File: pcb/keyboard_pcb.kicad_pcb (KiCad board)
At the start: 2 copper layers, 144.8 x 98.6 mm, 23 parts, among them J1 TRRS, K00 KEYSW, K01 KEYSW, K02 KEYSW, K03 KEYSW, K04 KEYSW, K05 KEYSW, K10 KEYSW, K11 KEYSW, K12 KEYSW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

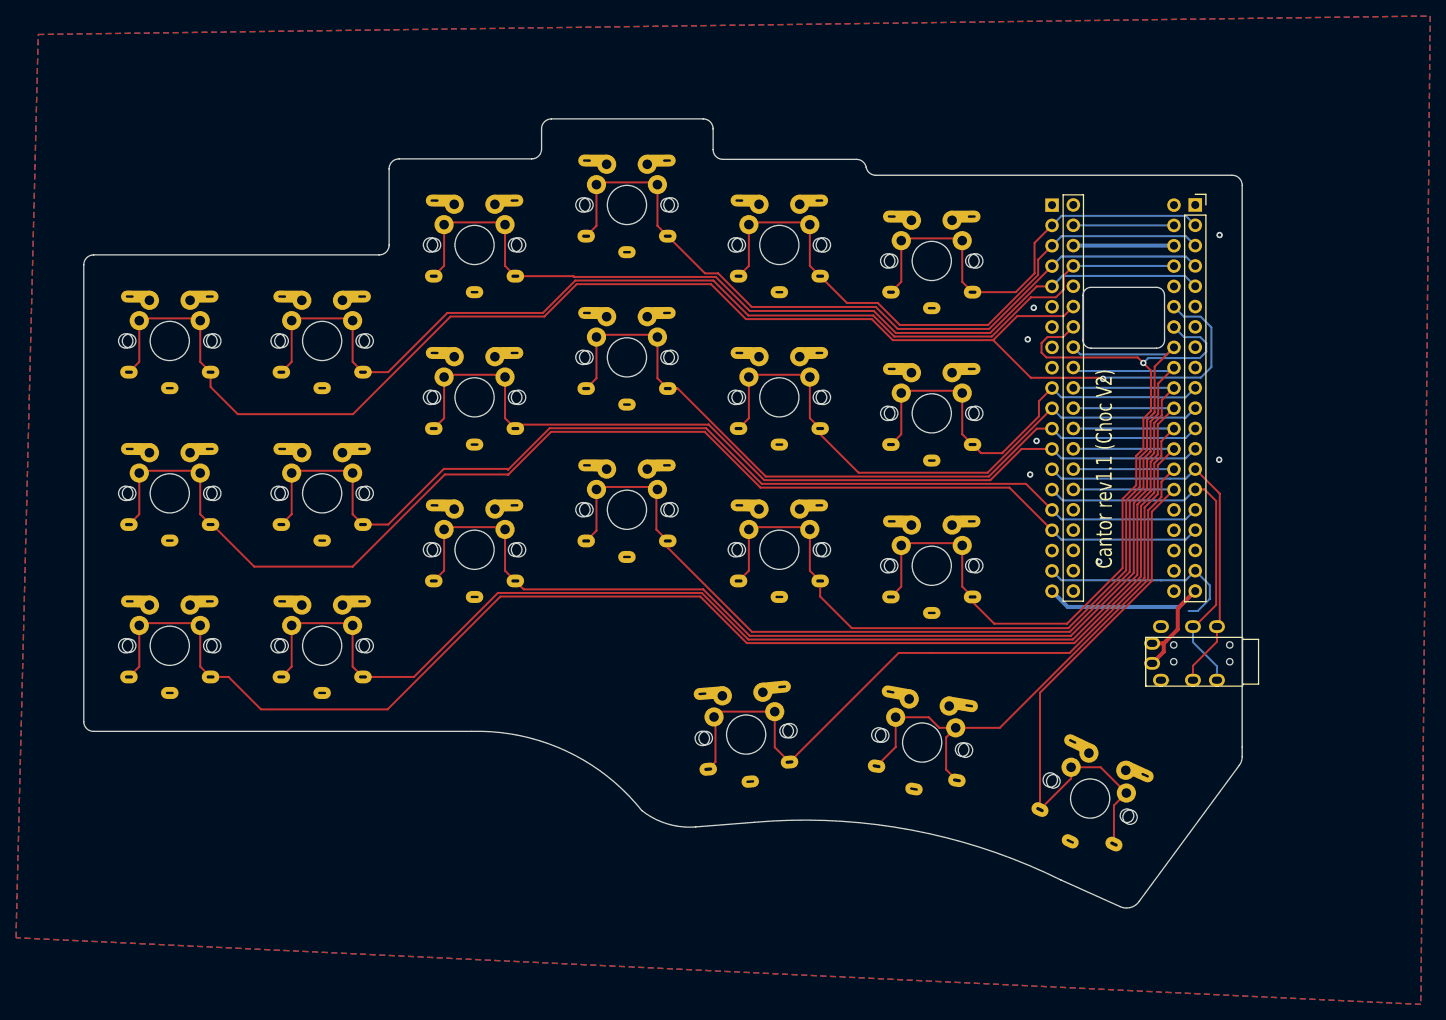
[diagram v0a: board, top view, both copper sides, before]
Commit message: Routing and edgecut cleanup, DRC error fixes
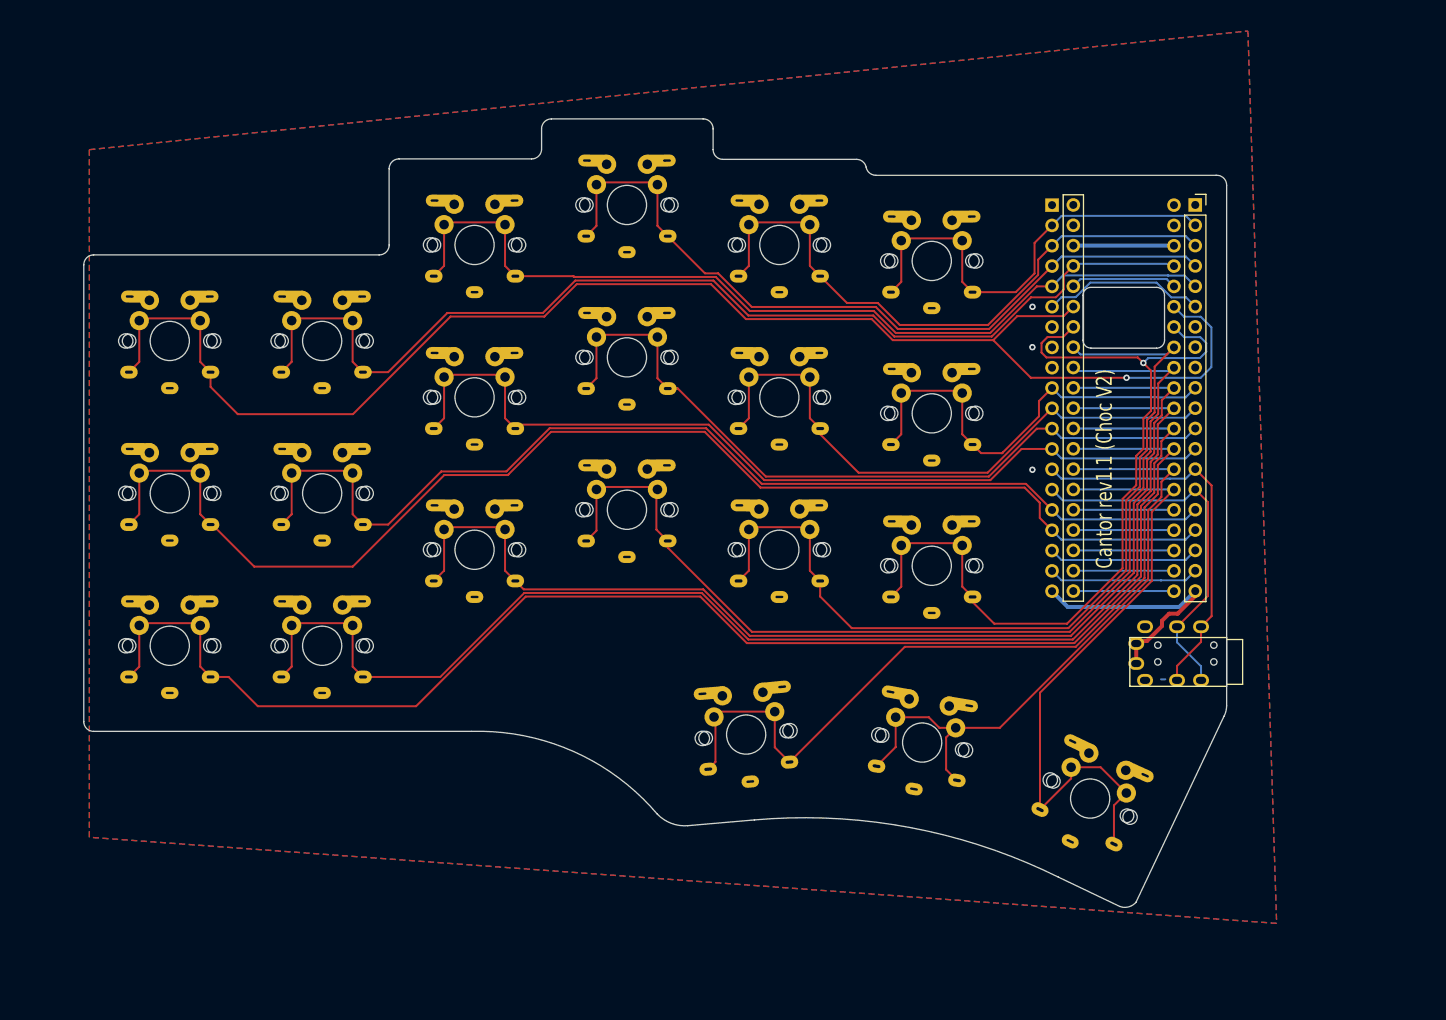
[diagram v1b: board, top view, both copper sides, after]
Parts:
- moved J1 1.99 mm to (200.9, 110.1)
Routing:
- net GND: track 41.3 -> 20.2 mm, vias 7 -> 3
- net unconnected-(U1-Pad6): track 0.00 -> 20.4 mm
- net unconnected-(U1-Pad18): track 0.00 -> 18.9 mm
- net unconnected-(U1-Pad36): track 0.00 -> 13.3 mm
- net unconnected-(U1-Pad25): track 0.00 -> 12.6 mm
- net unconnected-(U1-Pad24): track 0.00 -> 12.6 mm
- net unconnected-(U1-Pad23): track 0.00 -> 12.6 mm
- net unconnected-(U1-Pad22): track 0.00 -> 12.6 mm
- net unconnected-(U1-Pad21): track 0.00 -> 12.6 mm
- net /k10: track 160.1 -> 161.1 mm
- net /RX: track 47.2 -> 46.4 mm
- net +3V3: track 44.8 -> 45.5 mm
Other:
- board size 144.8 x 98.6 mm -> 142.9 x 98.6 mm

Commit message: Fixed drill layer misalingment and regenerated Gerbers
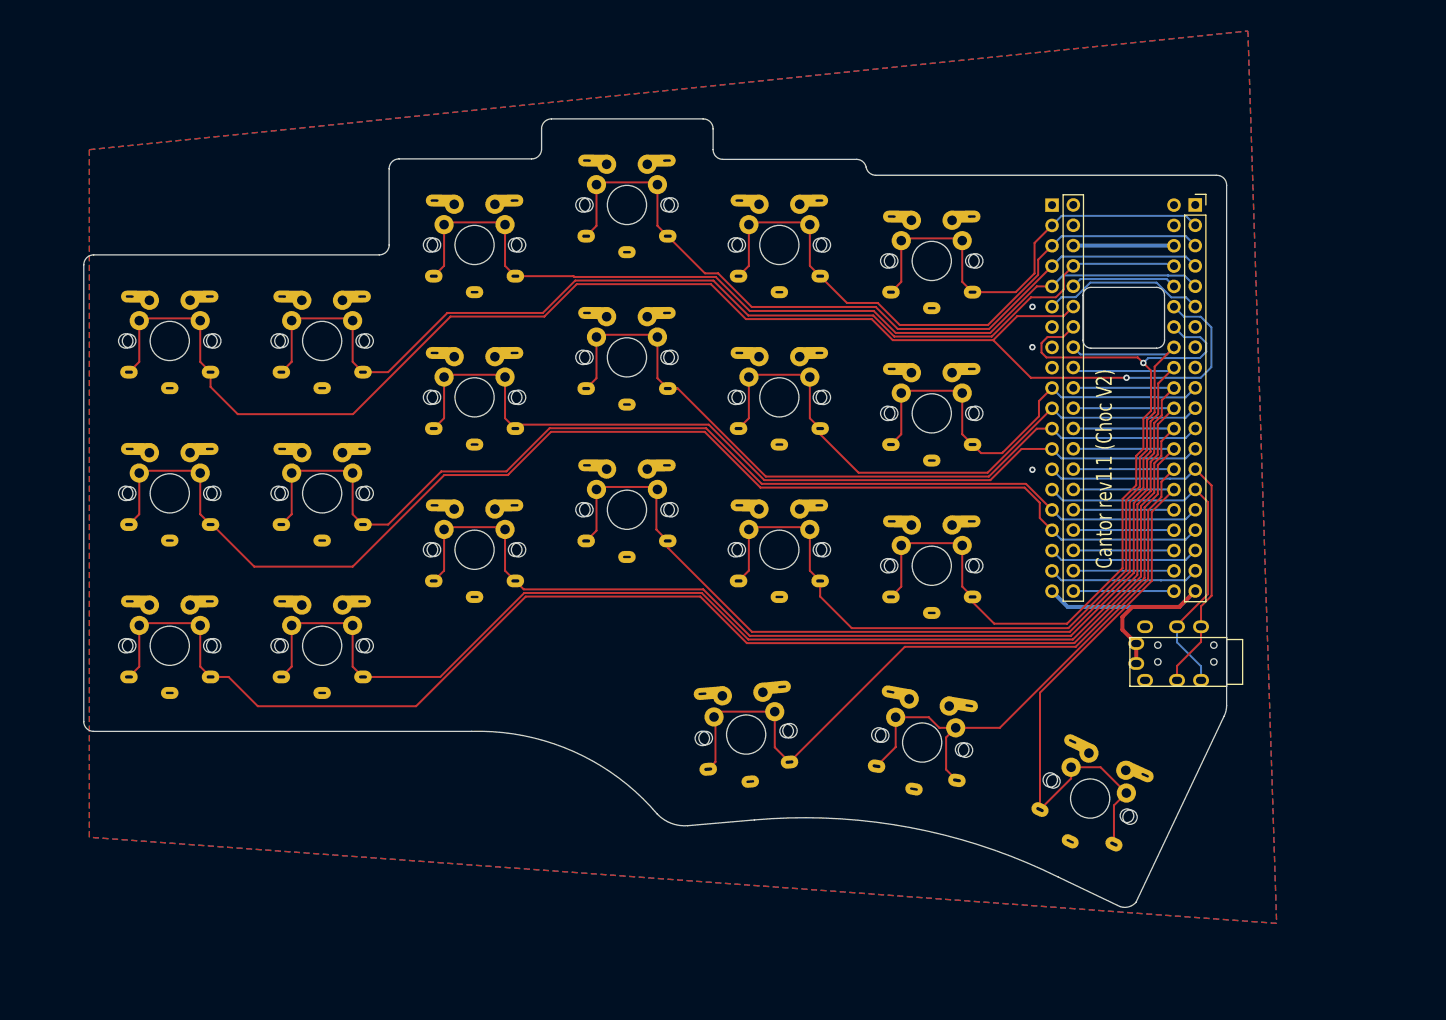
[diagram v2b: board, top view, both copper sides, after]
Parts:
- J1: footprint Keebio-Parts:TRRS-PJ-320A -> ergodonk_kicad_library:Cantor_DS_TRRS-PJ-320A
- U1: footprint Footprints:YAAJ_WeAct_BlackPill_2 -> ergodonk_kicad_library:Cantor_DS_YAAJ_WeAct_BlackPill_2
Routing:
- net +3V3: track 45.5 -> 49.1 mm
- net /k23: track 128.9 -> 126.7 mm
- net /k01: track 135.7 -> 134.2 mm
- net /k12: track 112.5 -> 111.0 mm
- net /k25: track 106.4 -> 104.9 mm
- net GND: track 20.2 -> 18.9 mm
- net /k30: track 106.1 -> 104.8 mm
- net /k15: track 55.7 -> 54.7 mm
- net /k02: track 113.3 -> 112.5 mm
- net /k24: track 110.3 -> 109.5 mm
- net /k22: track 143.0 -> 142.2 mm
- net /k21: track 164.0 -> 163.2 mm
- net /k20: track 183.9 -> 183.1 mm
- net /k05: track 56.1 -> 55.3 mm
- net /k14: track 75.7 -> 74.9 mm
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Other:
- outline, holes or cut-outs redrawn

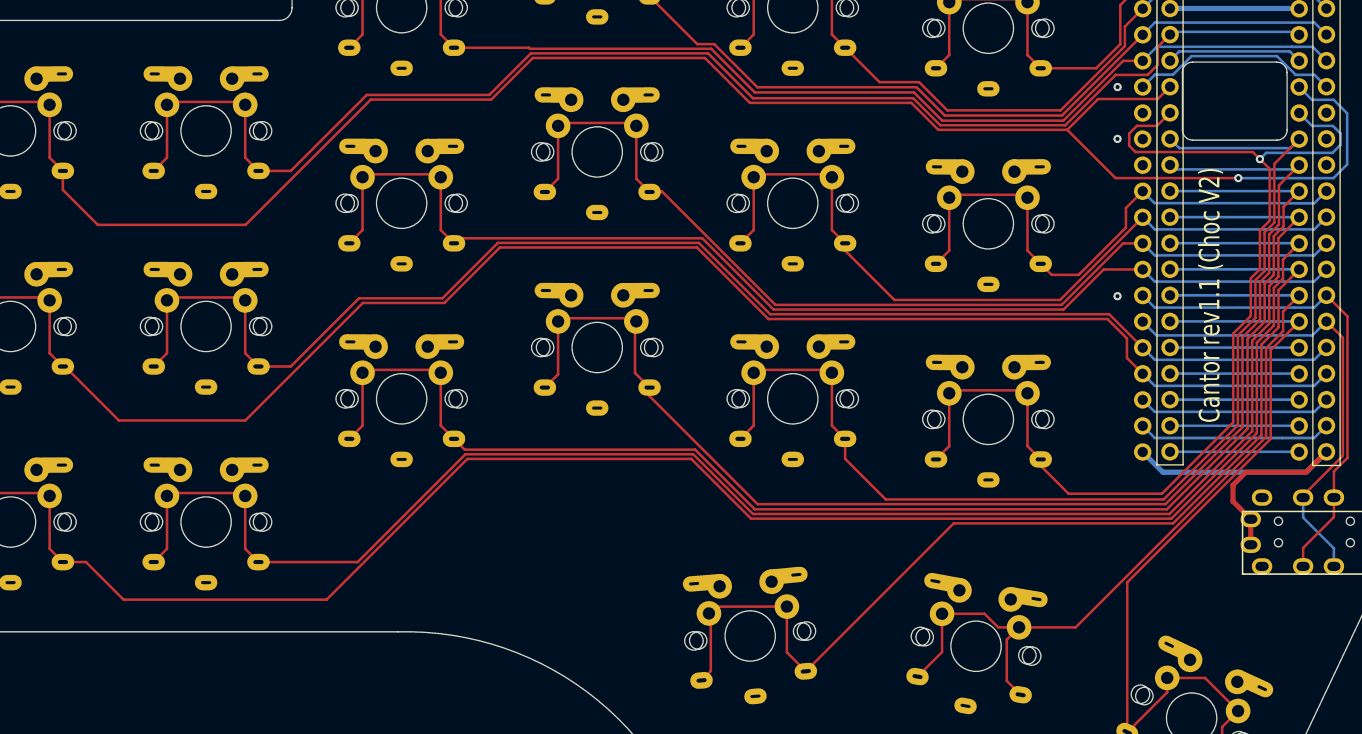
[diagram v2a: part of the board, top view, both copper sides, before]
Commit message: Added branding and rebuilt gerbers
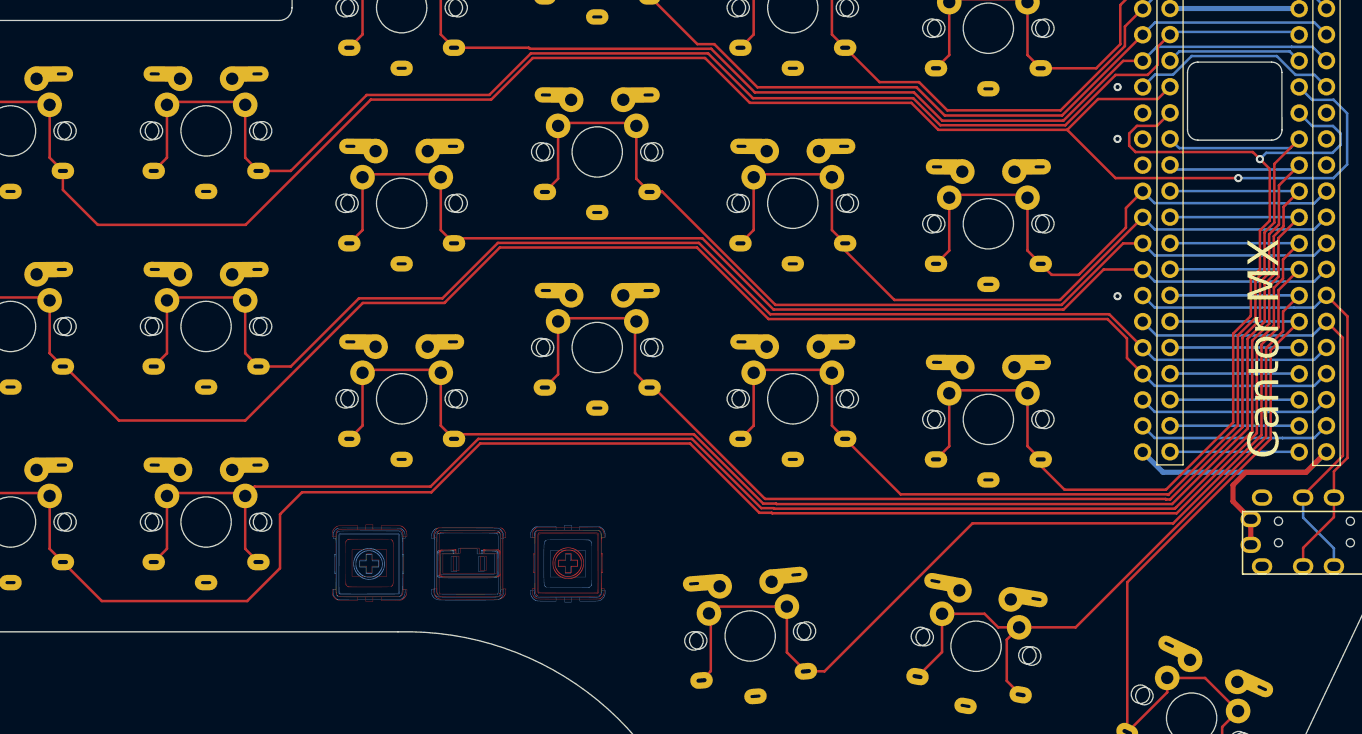
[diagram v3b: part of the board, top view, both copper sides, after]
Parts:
- added G***: LOGO, LOGO, F.Cu at (113.2, 112.0)
- added G***: LOGO, LOGO, B.Cu at (186.8, 83.2)
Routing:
- net /k20: track 183.1 -> 187.1 mm
- net /k24: track 109.5 -> 108.0 mm
- net /k23: track 126.7 -> 125.9 mm
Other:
- outline, holes or cut-outs redrawn
- board text added: "Cantor MX"
- board text added: "Cantor MX rev1.1 by JellyTitan"
- board text removed: "Cantor"
- board text removed: "Cantor rev1.1 (Choc V2)"

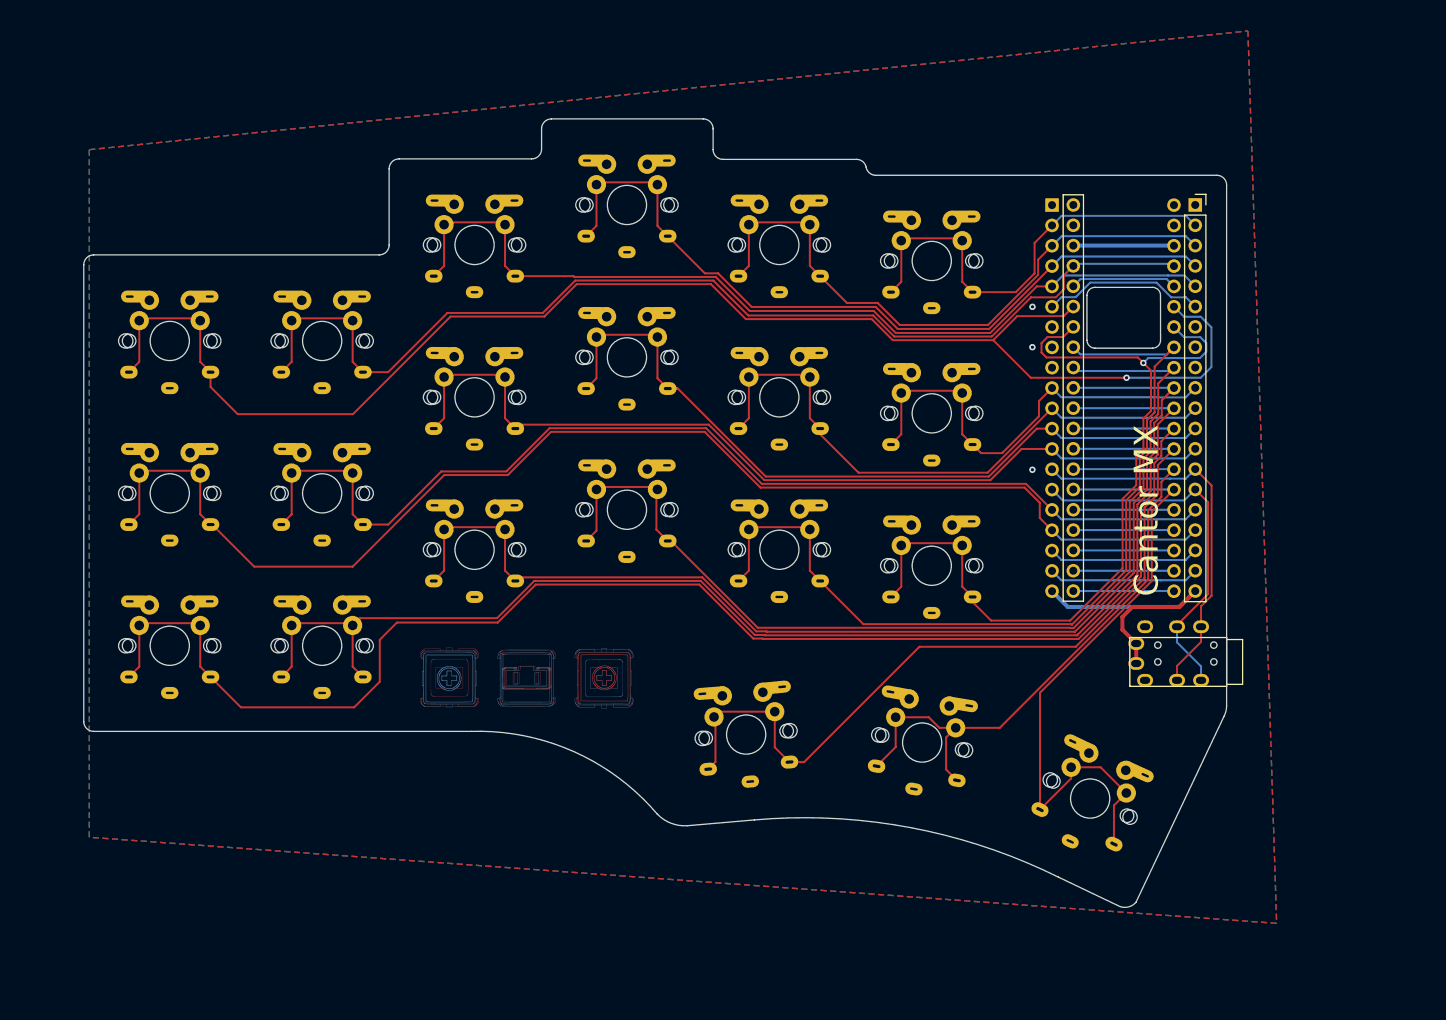
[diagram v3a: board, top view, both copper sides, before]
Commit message: Moved Blackpill l closer to top edge to accomidate wide-lipped usb-c
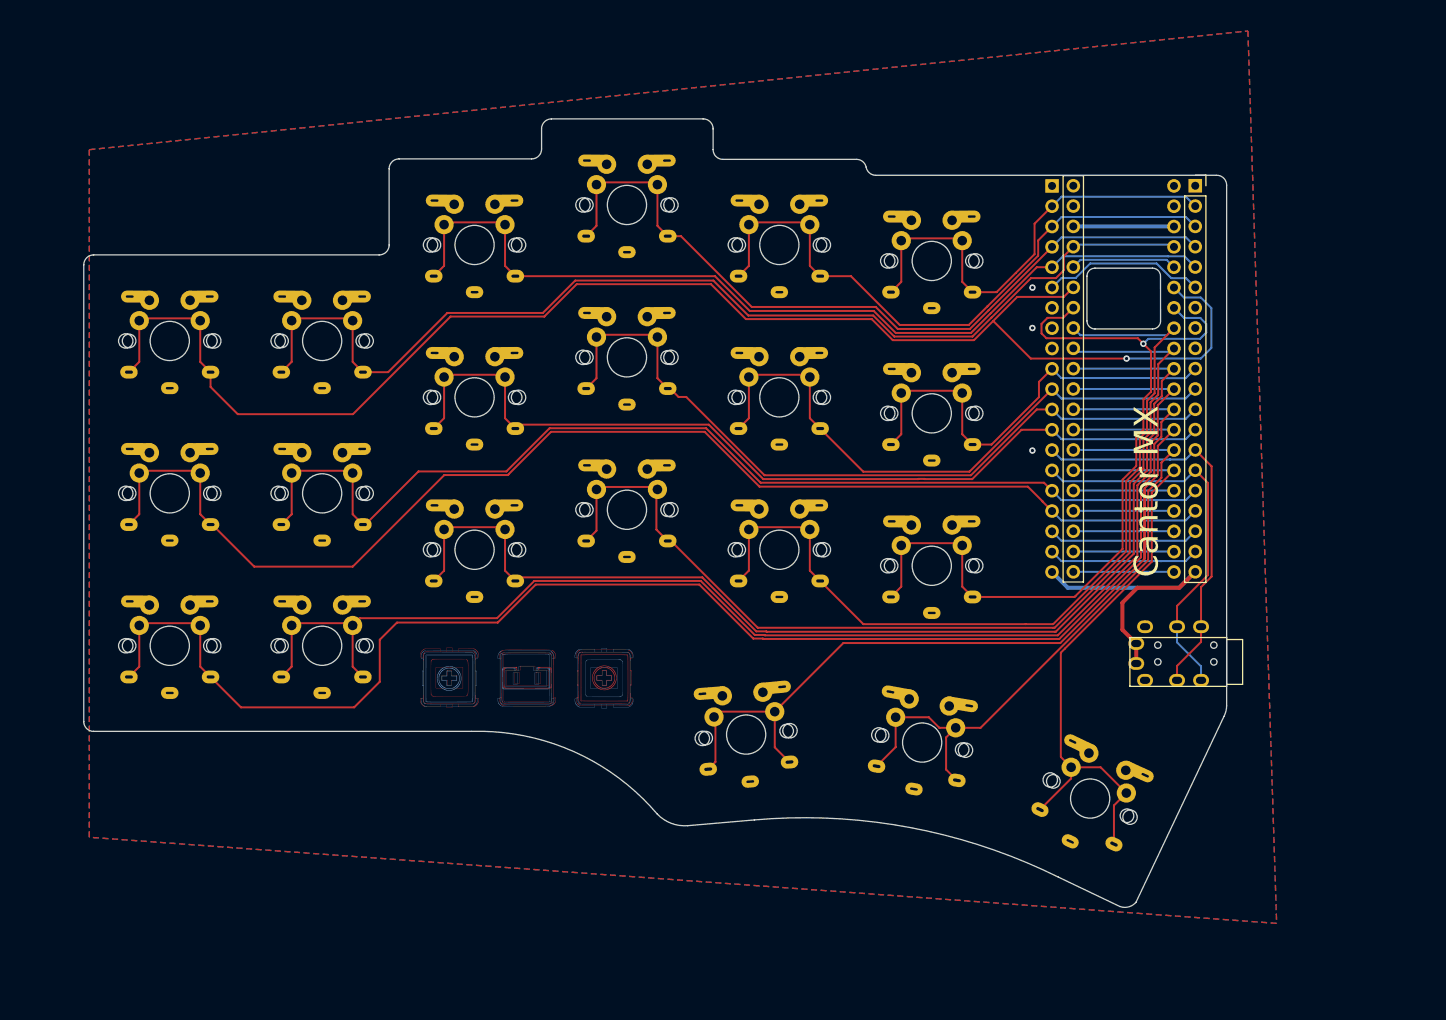
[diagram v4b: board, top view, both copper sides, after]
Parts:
- moved G*** 2.40 mm to (186.8, 80.8)
- moved U1 2.40 mm to (179.2, 50.6)
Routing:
- net /k30: track 104.8 -> 113.7 mm
- net /k32: track 81.7 -> 78.2 mm
- net /RX: track 46.2 -> 48.8 mm
- net /TX: track 47.9 -> 50.3 mm
- net /k10: track 160.3 -> 158.2 mm
- net +3V3: track 49.1 -> 51.1 mm
- net /k05: track 55.3 -> 56.5 mm
- net /k25: track 104.6 -> 103.4 mm
- net /k11: track 135.2 -> 134.2 mm
- net /k22: track 142.1 -> 143.1 mm
- net /k02: track 112.5 -> 113.5 mm
- net /k31: track 82.2 -> 83.2 mm
- net /k04: track 76.6 -> 77.6 mm
- net /k20: track 187.1 -> 188.1 mm
- net /k03: track 96.0 -> 97.0 mm
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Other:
- outline, holes or cut-outs redrawn
